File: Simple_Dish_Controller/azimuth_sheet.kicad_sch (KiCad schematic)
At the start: 21 parts, among them J3 1-Pin Terminal Block, J4 Conn_01x03_Pin, J5 RJ45 port shielded, RA, TH, J9 RJ45 port shielded, RA, TH, Q3 PZT2222A, Q4 PZT2222A, U2 74LS08, U3 74LS32, U5 NE555PS

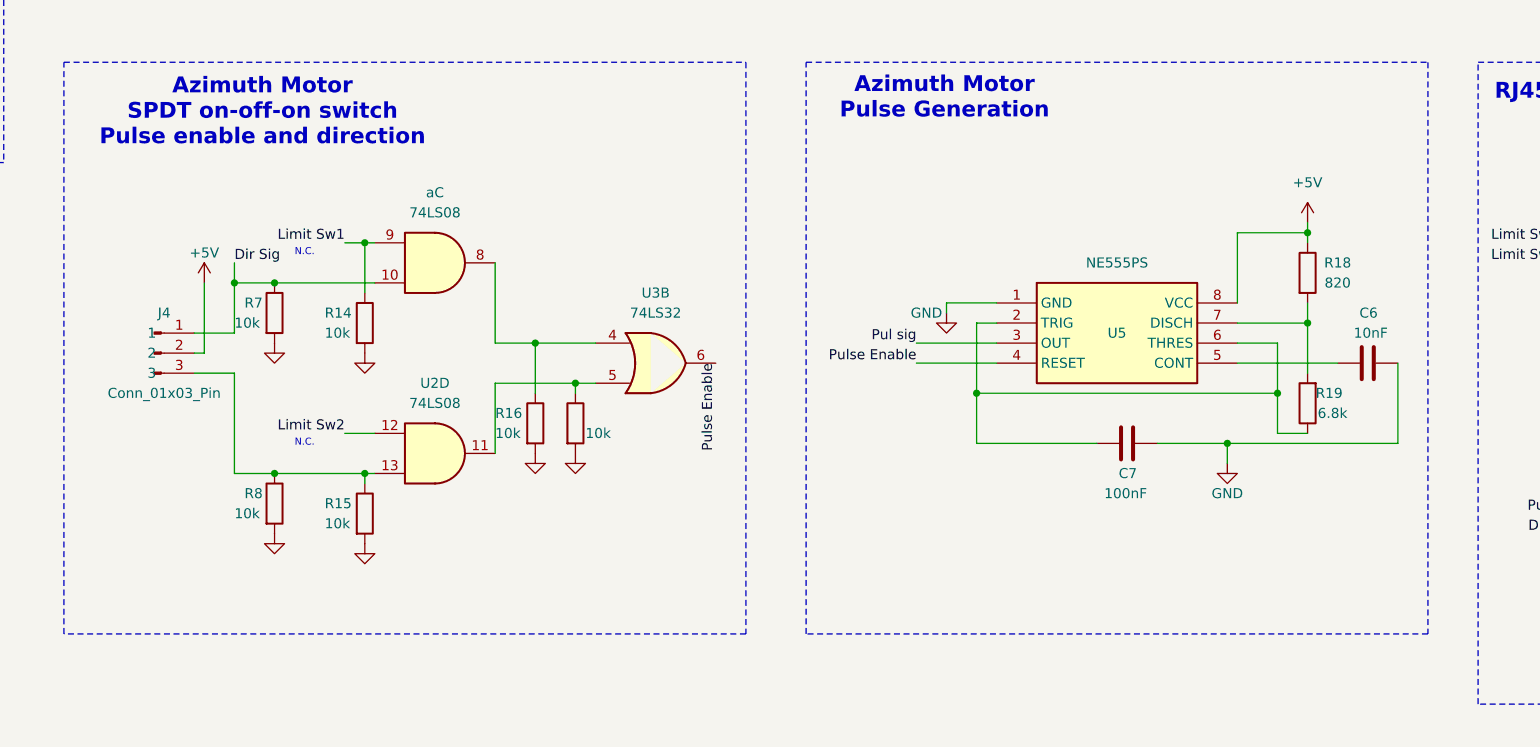
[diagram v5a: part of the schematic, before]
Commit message: More parts defined
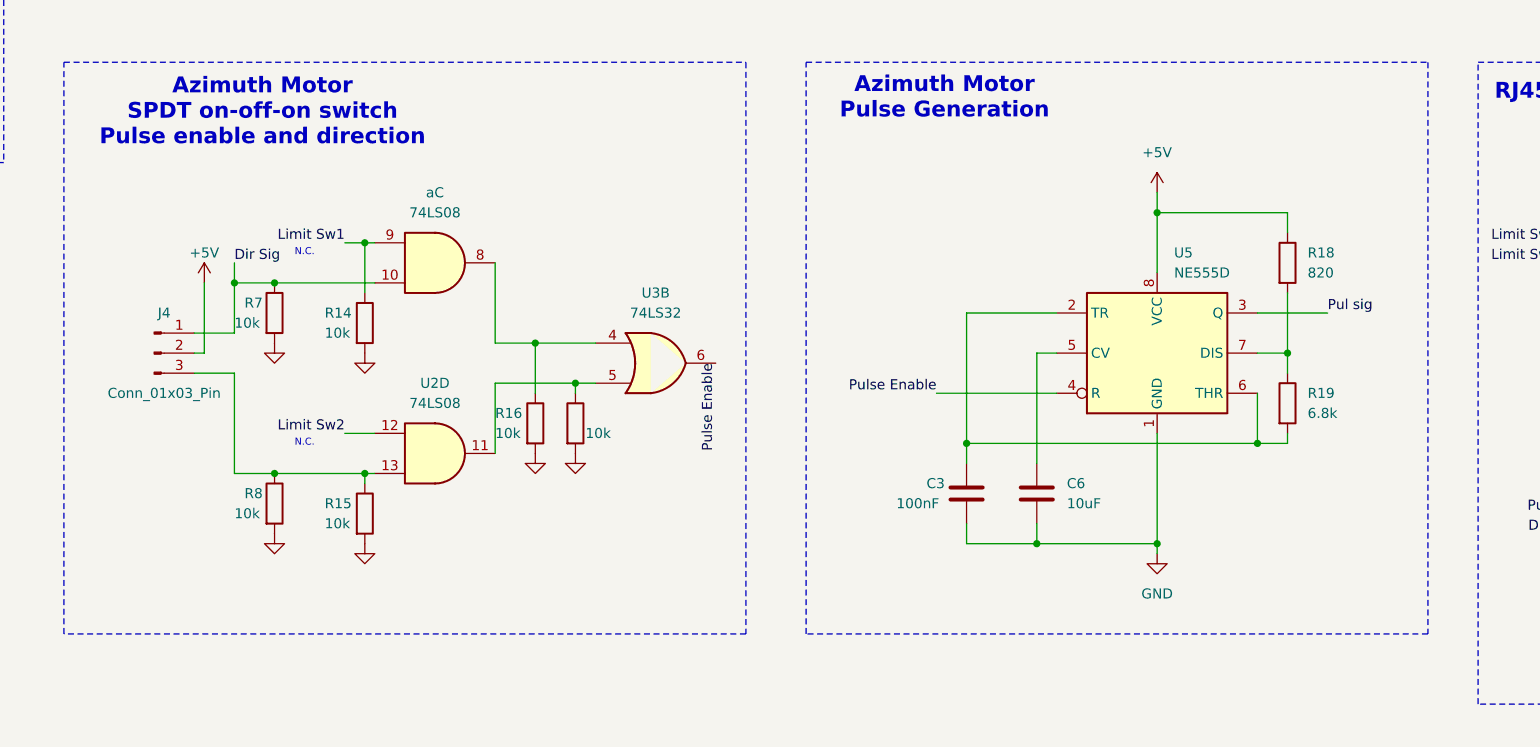
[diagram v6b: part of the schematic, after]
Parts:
- removed C6: 10nF, Capacitor_SMD:C_0805_2012Metric, symbol Device:C
- removed C7: 100nF, Capacitor_SMD:C_0805_2012Metric, symbol Device:C
- removed R18: 820, Resistor_SMD:R_0805_2012Metric, symbol Device:R
- removed R19: 6.8k, Resistor_SMD:R_0805_2012Metric, symbol Device:R
- removed U5: NE555PS, NE555P Osc Chip SMD:SOIC127P780X200-8N, symbol NE555P Osc Chip SMD:NE555PS
- added C3: 100nF, DishFootprints:C_0805, symbol DishSymbols:CAP 100nF 0805
- added C6: 10uF, DishFootprints:C_0805, symbol DishSymbols:CAP 10nF 0805
- added R18: 820, DishFootprints:R_0805, symbol DishSymbols:RES 820 0805
- added R19: 6.8k, DishFootprints:R_0805, symbol DishSymbols:RES 6.8k 0805
- added U5: NE555D, DishFootprints:SOIC-8_3.9x4.9mm_P1.27mm, symbol DishSymbols:NE555D
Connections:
- net +5V: now also R18.1, U5.8 (VCC)
- net GND: now also C3.2, C6.2, U5.1 (GND)
- net Pul sig: now also U5.3 (Q)
- net Pulse Enable: now also U5.4 (R)
- new net: C6.1, U5.5 (CV)
- new net: R18.2, R19.1, U5.7 (DIS)
- new net: C3.1, R19.2, U5.2 (TR), U5.6 (THR)

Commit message: Latest update
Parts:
- removed J3: 1-Pin Terminal Block, 1-Pin Barrier Terminal Block:RHDR1W160P0X826_1X1_1020X1270X1270P, symbol 1-Pin Barrier Terminal Block:38700-6301
- removed J5, J9: RJ45 port shielded, RA, TH, DishController_footprints:RJ45 Port Shielded, Right Angle TH, symbol DishController_symbols:RJ45 port shielded, Right Angle TH
- removed Q3, Q4: PZT2222A, Package_TO_SOT_SMD:SOT-223-3_TabPin2, symbol Transistor_BJT:PZT2222A
- removed U2, a: 74LS08, 74LS08_SOIC:SOIC127P600X175-14N, symbol 74xx:74LS08
- removed U3: 74LS32, 74LS32_SOIC:SOIC127P600X175-14N, symbol 74xx:74LS32
- added J3: DE-15_VGA_FEMALE_CONN, DishFootprintsSupplier:DB15_VGA_FEMALE_CONN, symbol DishSymbolsSupplier:DE-15_VGA_FEMALE_CONN
- added Q3, Q4: PZT2222A, DishFootprints:SOT-223, symbol DishSymbols:PZT2222A
- added U2: 74LS08, DishFootprints:SOIC-14_3.9x8.7mm_P1.27mm, symbol DishSymbols:74LS08
- added U3: 74LS32, DishFootprints:SOIC-14_3.9x8.7mm_P1.27mm, symbol DishSymbols:74LS32
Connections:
- net +5V: now also J3.1
- net Dir: now also J3.12, Q3.2 (C)
- net Dir Sig: now also U2.10
- net GND: now also J3.2, Q3.3 (E), Q4.3 (E)
- net Limit Sw1: now also J3.3, U2.9
- net Limit Sw2: now also J3.4, U2.12
- net Pul: now also J3.11, Q4.2 (C)
- net Pul sig: now also Q4.1 (B)
- net Pulse Enable: now also U3.6
- net Shield: now also J3.SH1 (SHIELD), J3.SH2 (SHIELD)
- net at R16.1: now also U2.8, U3.4
- net at R17.1: now also U2.11, U3.5
- net at J4.3, R15.1, R8.1: now also U2.13
- net at R9.2: now also Q3.1 (B)
- no-connect marks 16 -> 9
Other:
- note removed: "Connect to Chassis"
- note removed: "Shield to Chassis"

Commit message: Updates
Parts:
- removed C3: 100nF, DishFootprints:C_0805, symbol DishSymbols:CAP 100nF 0805
- removed C6: 10uF, DishFootprints:C_0805, symbol DishSymbols:CAP 10nF 0805
- removed J3: DE-15_VGA_FEMALE_CONN, DishFootprintsSupplier:DB15_VGA_FEMALE_CONN, symbol DishSymbolsSupplier:DE-15_VGA_FEMALE_CONN
- removed J4: Conn_01x03_Pin, DishFootprints:PinHeader_1x03_P2.54mm_Vertical, symbol DishSymbols:Conn_01x03_Pin
- removed Q3, Q4: PZT2222A, DishFootprints:SOT-223, symbol DishSymbols:PZT2222A
- removed R18: 820, DishFootprints:R_0805, symbol DishSymbols:RES 820 0805
- removed R19: 6.8k, DishFootprints:R_0805, symbol DishSymbols:RES 6.8k 0805
- removed R7, R8: 10k, Resistor_SMD:R_0805_2012Metric, symbol Device:R
- removed R9: 1k, Resistor_SMD:R_0805_2012Metric, symbol Device:R
- removed U2: 74LS08, DishFootprints:SOIC-14_3.9x8.7mm_P1.27mm, symbol DishSymbols:74LS08
- removed U3: 74LS32, DishFootprints:SOIC-14_3.9x8.7mm_P1.27mm, symbol DishSymbols:74LS32
- removed U5: NE555D, DishFootprints:SOIC-8_3.9x4.9mm_P1.27mm, symbol DishSymbols:NE555D
- added C10: 10uF, Capacitor_SMD:C_1206_3216Metric, symbol Device:C
- added C8: 0.1uF, Capacitor_SMD:C_1206_3216Metric, symbol Device:C
- added C9: 100nF, Capacitor_SMD:C_1206_3216Metric, symbol Device:C
- added J6: Conn_01x03_Pin, Connector_PinHeader_2.54mm:PinHeader_1x03_P2.54mm_Vertical, symbol Connector:Conn_01x03_Pin
- added J7: Azimuth DE-15, DishFootprints:DE15_VGA_FEMALE_CONN, symbol DishSymbols:DE-15_VGA_FEMALE_CONN
- added Q3, Q4: MMBT2222A, Package_TO_SOT_SMD:SOT-23, symbol Transistor_BJT:MMBT2222A
- added R11: 820, Resistor_SMD:R_1206_3216Metric, symbol Device:R
- added R12, R13, R18: 10k, Resistor_SMD:R_1206_3216Metric, symbol Device:R
- added R19: 1k, Resistor_SMD:R_1206_3216Metric, symbol Device:R
- added U2: 74LS32, Package_SO:SOIC-14_3.9x8.7mm_P1.27mm, symbol 74xx:74LS32
- added U3: 74LS08, Package_SO:SOIC-14_3.9x8.7mm_P1.27mm, symbol 74xx:74LS08
- added U5: NE555D, Package_SO:SOIC-8_3.9x4.9mm_P1.27mm, symbol Timer:NE555D
- R14: value 10k -> 6.8k; footprint Resistor_SMD:R_0805_2012Metric -> Resistor_SMD:R_1206_3216Metric
- R15, R16, R17: footprint Resistor_SMD:R_0805_2012Metric -> Resistor_SMD:R_1206_3216Metric
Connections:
- net +5V: now also C8.1, J6.2 (Pin_2), J7.1, R11.2, U5.8 (VCC)
- net Dir: now also J7.12, Q3.3 (C)
- net Dir Sig: now also J6.1 (Pin_1), R12.1, R19.1, U3.10
- net GND: now also C10.2, C8.2, C9.2, J7.2, Q3.2 (E), Q4.2 (E), R12.2, R13.2, R18.2, U5.1 (GND); no longer R14.2
- net Limit Sw1: now also J7.3, R13.1, U3.9; no longer R14.1
- net Limit Sw2: now also J7.4, U3.12
- net Pul: now also J7.11, Q4.3 (C)
- net Pul sig: now also Q4.1 (B), U5.3 (Q)
- net Pulse Enable: now also U2.6, U5.4 (R)
- net Shield: now also J7.SH1 (SHIELD), J7.SH2 (SHIELD)
- net at R15.1: now also U2.4, U3.8
- net at R17.1: now also J6.3 (Pin_3), R18.1, U3.13
- net at R16.1: now also U2.5, U3.11
- new net: Q3.1 (B), R19.2
- new net: C9.1, R14.1, U5.2 (TR), U5.6 (THR)
- new net: R11.1, R14.2, U5.7 (DIS)
- new net: C10.1, U5.5 (CV)
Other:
- note added: "DE-15 Connector"
- note removed: "RJ45 Ports"
